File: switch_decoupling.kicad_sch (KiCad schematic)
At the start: 54 parts

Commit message: CuPhy: adding ports
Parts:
- C93: renamed from C21; manf# (none) -> C0603C475K8PACTU
- C94: renamed from C49; manf# (none) -> C0603C475K8PACTU
- renumbered C51 to C100, C3 to C101, C34 to C102, C52 to C103, C4 to C104, C35 to C105, C53 to C106, C5 to C107, C36 to C108, C54 to C109, C6 to C110, C37 to C111, C55 to C112, C7 to C113, C38 to C114, C56 to C115, C8 to C116, C39 to C117, C57 to C118, C9 to C119, C40 to C120, C58 to C121, C10 to C122, C41 to C123, C59 to C124, C11 to C125, C42 to C126, C60 to C127, C12 to C128, C43 to C129, C61 to C130, C13 to C131, C44 to C132, C62 to C133, C14 to C134, C45 to C135, C63 to C136, C15 to C137, C46 to C138, C64 to C139, C16 to C140, C47 to C141, C65 to C142, C17 to C143, C48 to C144, C66 to C145, C18 to C146, C1 to C95, C32 to C96, C50 to C97, C2 to C98, C33 to C99
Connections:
- net +1V1 renamed 1V1
- net +2V5 renamed 2V5
- net +3V3 renamed 3V3
- removed net GNDD: C100.2, C101.2, C102.2, C103.2, C104.2, C105.2, C106.2, C107.2, C108.2, C109.2, C110.2, C111.2, C112.2, C113.2, C114.2, C115.2, C116.2, C117.2, C118.2, C119.2, C120.2, C121.2, C122.2, C123.2, C124.2, C125.2, C126.2, C127.2, C128.2, C129.2, C130.2, C131.2, C132.2, C133.2, C134.2, C135.2, C136.2, C137.2, C138.2, C139.2, C140.2, C141.2, C142.2, C143.2, C144.2, C145.2, C146.2, C93.2, C94.2, C95.2, C96.2, C97.2, C98.2, C99.2
- new net: C102.2, C105.2, C108.2, C111.2, C114.2, C117.2, C120.2, C123.2, C126.2, C129.2, C132.2, C135.2, C138.2, C141.2, C144.2, C93.2, C96.2, C99.2
- new net: C101.2, C104.2, C107.2, C110.2, C113.2, C116.2, C119.2, C122.2, C125.2, C128.2, C131.2, C134.2, C137.2, C140.2, C143.2, C146.2, C95.2, C98.2
- new net: C100.2, C103.2, C106.2, C109.2, C112.2, C115.2, C118.2, C121.2, C124.2, C127.2, C130.2, C133.2, C136.2, C139.2, C142.2, C145.2, C94.2, C97.2

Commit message: schematics: fixing the voltage rail and updating the files
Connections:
- net 1V1 renamed 1V15
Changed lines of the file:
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@@
 		)
 	)
-	(hierarchical_label "1V1"
+	(hierarchical_label "1V15"
 		(shape bidirectional)
 		(at 27.94 36.83 180)

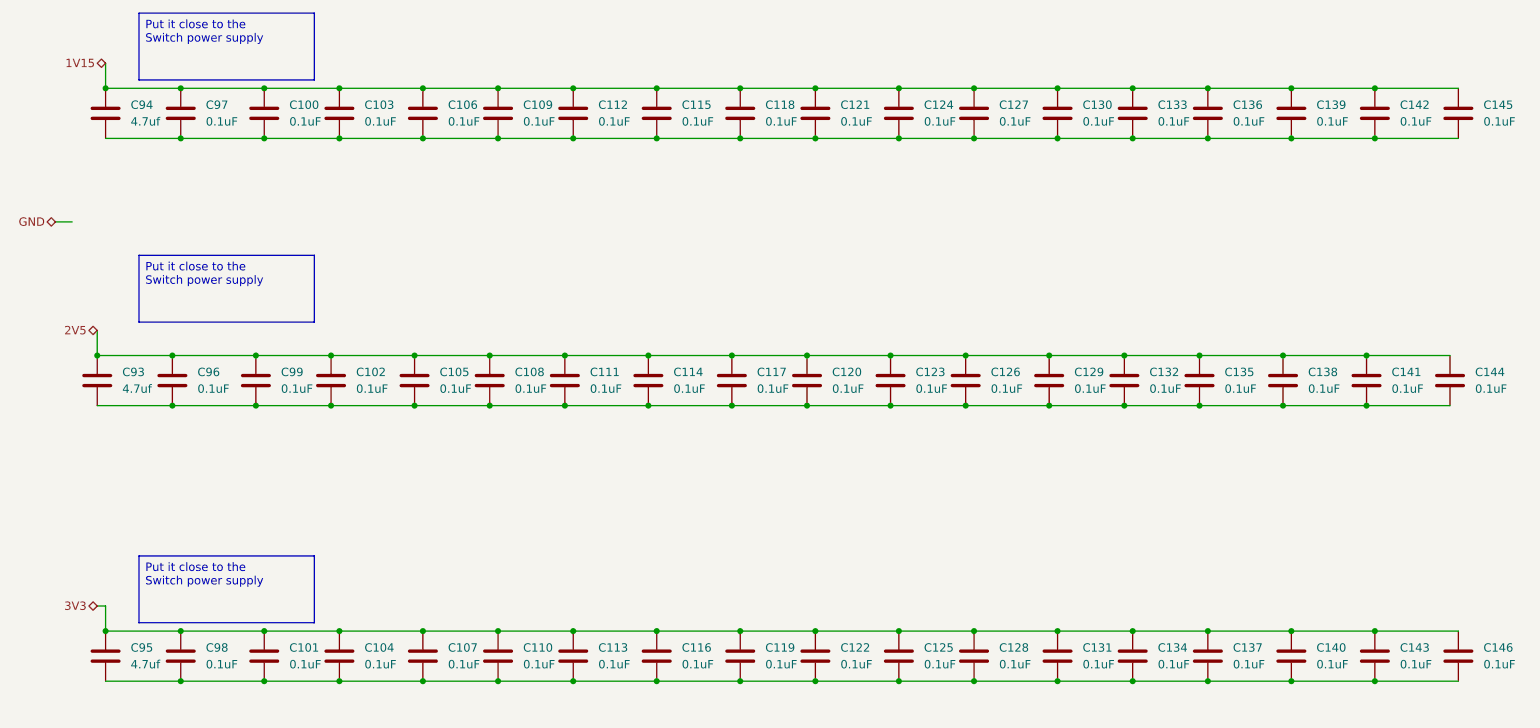
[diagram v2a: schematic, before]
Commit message: switch: finished 1st version
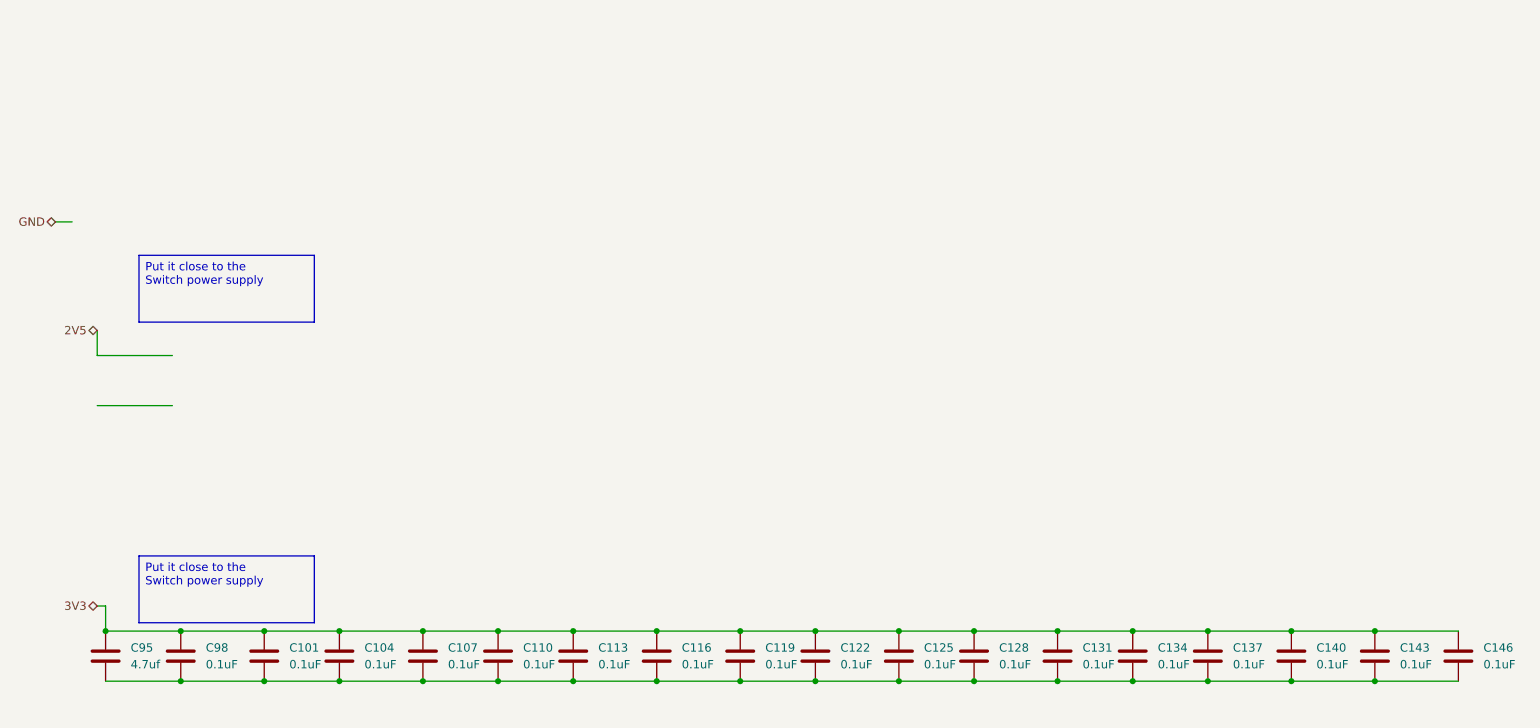
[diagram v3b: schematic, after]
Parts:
- removed C100, C102, C103, C105, C106, C108, C109, C111, C112, C114, C115, C117, C118, C120, C121, C123, C124, C126, C127, C129, C130, C132, C133, C135, C136, C138, C139, C141, C142, C144, C145, C96, C97, C99: 0.1uF, Capacitor_SMD:C_0805_2012Metric_Pad1.18x1.45mm_HandSolder, symbol Device:C
- removed C93, C94: 4.7uf, Capacitor_SMD:C_0805_2012Metric_Pad1.18x1.45mm_HandSolder, symbol Device:C
